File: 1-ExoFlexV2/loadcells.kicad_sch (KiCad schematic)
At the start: 60 parts, among them J75 Tulip Conn, J76 Tulip Conn, J77 Tulip Conn, J78 Tulip Conn, J79 Tulip Conn, J80 Tulip Conn, J81 Jumper, J82 Jumper, J83 Jumper, J84 Jumper, J85 Jumper, J86 Jumper, U25 INST OP-AMP, U26 INST OP-AMP, U27 INST OP-AMP, U28 COMP, U29 COMP, U30 COMP, U31 OR Gate, U32 OR Gate

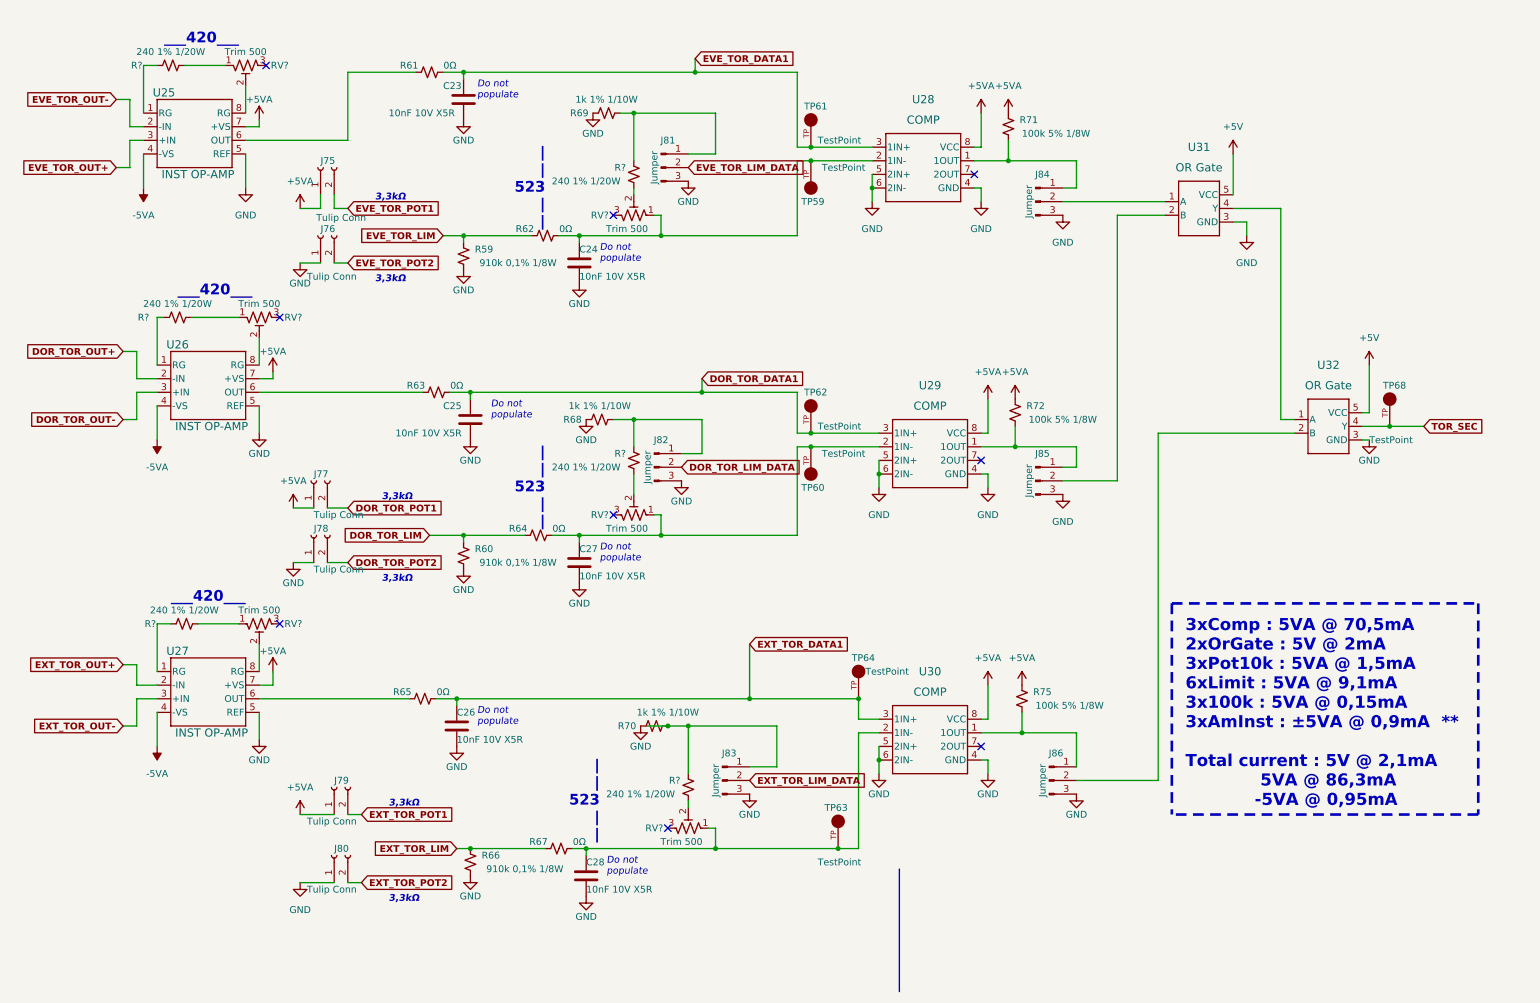
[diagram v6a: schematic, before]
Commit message: Finalisation schéma FIN
- Changement des uméro pour les inverseurs
- Changement des connecteur et début de placement
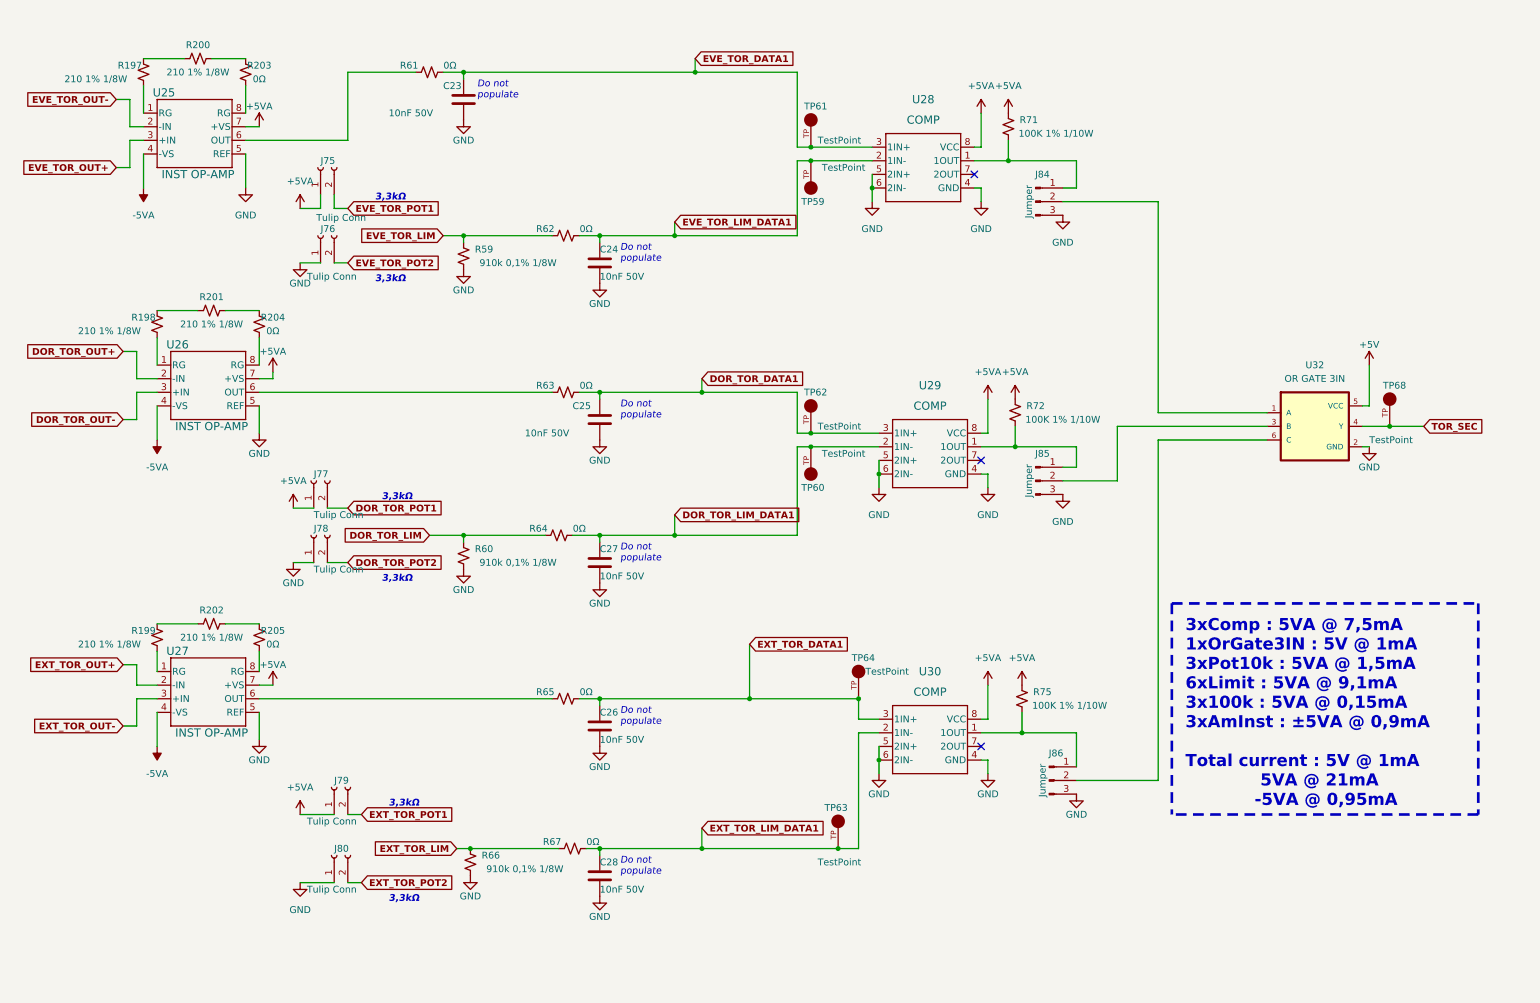
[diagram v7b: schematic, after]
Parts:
- removed J81, J82, J83: Jumper, Connector_PinHeader_2.54mm:PinHeader_1x03_P2.54mm_Vertical, symbol Connector:Conn_01x03_Male
- removed R68, R69, R70: 1k 1% 1/10W, Resistor_SMD:R_0402_1005Metric, symbol Device:R_Small_US
- removed R? (x6): 240 1% 1/20W, Resistor_SMD:R_0201_0603Metric, symbol Device:R_Small_US
- removed RV? (x6): Trim 500, FootPrint:TRIM_3296W-1-501LF, symbol Device:R_Potentiometer_Trim_US
- removed U31, U32: OR Gate, FootPrint:SOT95P270X145-5N, symbol SymLib:SN74LVC1G32DBVR
- added R197, R198, R199, R200, R201, R202: 210 1% 1/8W, Resistor_SMD:R_0805_2012Metric, symbol Device:R_Small_US
- added R203, R204, R205: 0Ω, Resistor_SMD:R_0805_2012Metric, symbol Device:R_Small_US
- added U32: OR GATE 3IN, FootPrintLib:SOT95P280X145-6N, symbol SymLib:SN74LVC1G332DBVR
- C23, C24, C25, C26, C27, C28: value 10nF 10V X5R -> 10nF 50V; footprint Capacitor_SMD:C_0603_1608Metric -> Capacitor_SMD:C_0805_2012Metric; DESCRIPTION 10000 pF ±5% 10V Ceramic Capacitor U2J 0603 (1608 Metric) -> 10000 pF ±5% 50V Ceramic Capacitor C0G, NP0 0805 (2012 Metr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; PACKAGE 0603 (1608 Metric) -> 0805 (2012 Metric); PART NUMBER GRM1857U1A103JA44D -> GRM2195C1H103JA01D
- R71, R72, R75: value 100k 5% 1/8W -> 100K 1% 1/10W; footprint Resistor_SMD:R_0805_2012Metric -> Resistor_SMD:R_0603_1608Metric; DESCRIPTION 100 kOhms ±5% 0.125W, 1/8W Chip Resistor 0805 (2012 Metric)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 -> 100 kOhms ±1% 0.1W, 1/10W Chip Resistor 0603 (1608 Metric) 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; PACKAGE 0805 (2012 Metric) -> 0603 (1608 Metric); PART NUMBER ERJ-6GEYJ104V -> ERJ-3EKF1003V
- TP59, TP60, TP61, TP62, TP63, TP64, TP68: NOTES (none) -> DO NOT POPULATE; PURCHASE-URL https://pricing.snapeda.com/search/part/5005/?ref=eda -> (none)
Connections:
- net +5V: now also U32.5 (VCC)
- net GND: now also U32.2 (GND)
- net TOR_SEC: now also U32.4 (Y)
- net EXT_TOR_LIM_DATA1: now reaches C28.1, R67.2, TP63.TP, U30.2 (1IN-)
- net EVE_TOR_LIM_DATA1: now reaches C24.1, R62.2, TP59.TP, U28.2 (1IN-)
- net at U26.1 (RG): now also R198.1
- net at U26.8 (RG): now also R204.2
- net DOR_TOR_LIM_DATA1: now reaches C27.1, R64.2, TP60.TP, U29.2 (1IN-)
- net at U25.1 (RG): now also R197.1
- net at U25.8 (RG): now also R203.2
- net at J86.2 (Pin_2): now also U32.6 (C)
- net at J84.2 (Pin_2): now also U32.1 (A)
- net at U27.1 (RG): now also R199.1
- net at U27.8 (RG): now also R205.2
- net at J85.2 (Pin_2): now also U32.3 (B)
- new net: R198.2, R201.1
- new net: R201.2, R204.1
- new net: R200.2, R203.1
- new net: R197.2, R200.1
- new net: R199.2, R202.1
- new net: R202.2, R205.1
- no-connect marks 9 -> 3
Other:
- note added: "3xComp : 5VA @ 7,5mA 1xOrGate3IN : 5V @ 1mA 3xPot10k : 5VA @ 1,5mA 6xLimit : 5VA @ 9,1mA 3x100k : 5VA @ 0,15mA 3xAmInst : ±5VA @ 0,9mA Total current : 5V @ 1mA 5VA @ 21mA -5VA @ 0,95mA"
- note removed: "3xComp : 5VA @ 70,5mA 2xOrGate : 5V @ 2mA 3xPot10k : 5VA @ 1,5mA 6xLimit : 5VA @ 9,1mA 3x100k : 5VA @ 0,15mA 3xAmInst : ±5VA @ 0,9mA ** Total current : 5V @ 2,1mA 5VA @ 86,3mA -5VA @ 0,95mA"
- note removed: "___420___"
- note removed: "| | 523 | |"
- moved on the sheet: C24, C25, C26, C27, C28, R62, R63, R64, R65, R67

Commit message: Modification Schéma + Layout
- Ajout de RC potentiel entre les capteur de torque et l'ampli d'instru
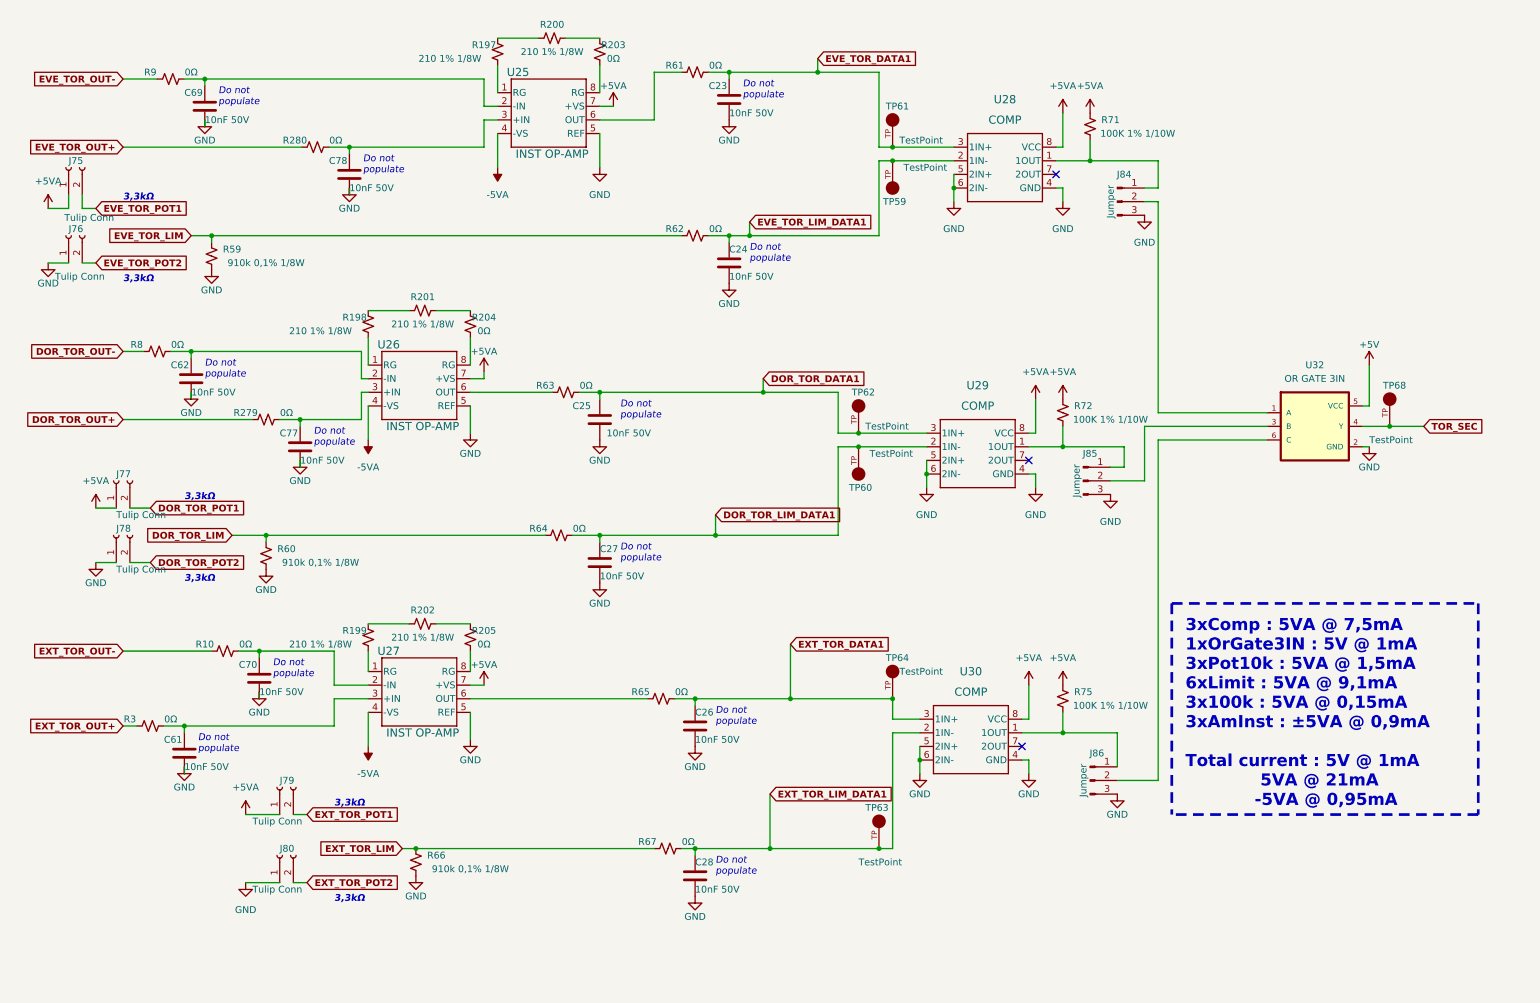
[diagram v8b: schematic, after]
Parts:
- added C61, C62, C69, C70, C77, C78: 10nF 50V, Capacitor_SMD:C_0805_2012Metric, symbol Device:C
- added R10, R279, R280, R3, R8, R9: 0Ω, Resistor_SMD:R_0805_2012Metric, symbol Device:R_Small_US
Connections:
- net DOR_TOR_OUT+: now also R279.1; no longer U26.2 (-IN)
- net DOR_TOR_OUT-: now also R8.1; no longer U26.3 (+IN)
- net EVE_TOR_OUT+: now also R280.1; no longer U25.3 (+IN)
- net EVE_TOR_OUT-: now also R9.1; no longer U25.2 (-IN)
- net EXT_TOR_OUT+: now also R3.1; no longer U27.2 (-IN)
- net EXT_TOR_OUT-: now also R10.1; no longer U27.3 (+IN)
- net GND: now also C61.2, C62.2, C69.2, C70.2, C77.2, C78.2
- new net: C62.1, R8.2, U26.2 (-IN)
- new net: C77.1, R279.2, U26.3 (+IN)
- new net: C69.1, R9.2, U25.2 (-IN)
- new net: C78.1, R280.2, U25.3 (+IN)
- new net: C70.1, R10.2, U27.2 (-IN)
- new net: C61.1, R3.2, U27.3 (+IN)
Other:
- moved on the sheet: C23, C24, C26, C28, J75, J76, J77, J78, J79, J80, J84, J85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
